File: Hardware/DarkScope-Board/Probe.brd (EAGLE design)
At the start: 65.5 x 80 mm, 50 parts, among them IC1 TL084D, X1 1-227161-0, X4 2540-5

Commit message: Routed Probe Board
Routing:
- net GND: track 0.00 -> 321.7 mm, vias 0 -> 1
- net +5V: track 0.00 -> 157.5 mm, vias 0 -> 3
- net -5V: track 0.00 -> 99.2 mm
- net TRIG: track 0.00 -> 95.5 mm
- net ADCIN: track 0.00 -> 90.4 mm
- net VSENSEL1: track 0.00 -> 90.3 mm
- net TL_PWM: track 0.00 -> 65.7 mm
- net N$8: track 0.00 -> 64.0 mm
- net N$5: track 0.00 -> 61.8 mm
- net CPLSEL: track 0.00 -> 61.0 mm
- net N$6: track 0.00 -> 58.9 mm
- net N$7: track 0.00 -> 48.9 mm
- net N$24: track 0.00 -> 44.3 mm, vias 0 -> 2
- net N$1: track 0.00 -> 41.9 mm
- net N$20: track 0.00 -> 39.0 mm
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- added copper zone on layer 1, net GND
- added copper zone on layer 16, net GND

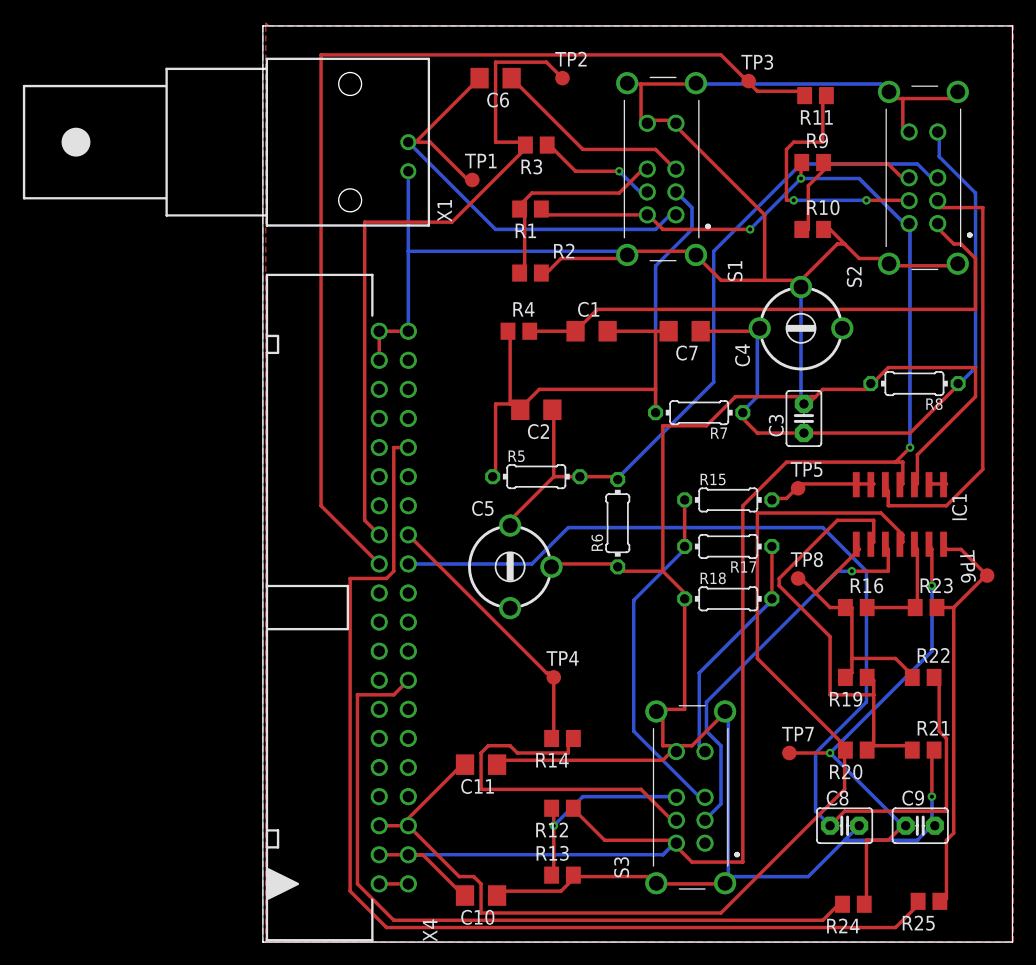
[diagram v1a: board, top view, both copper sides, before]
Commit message: Cleared and Fixed Probe Board's ERC Errors
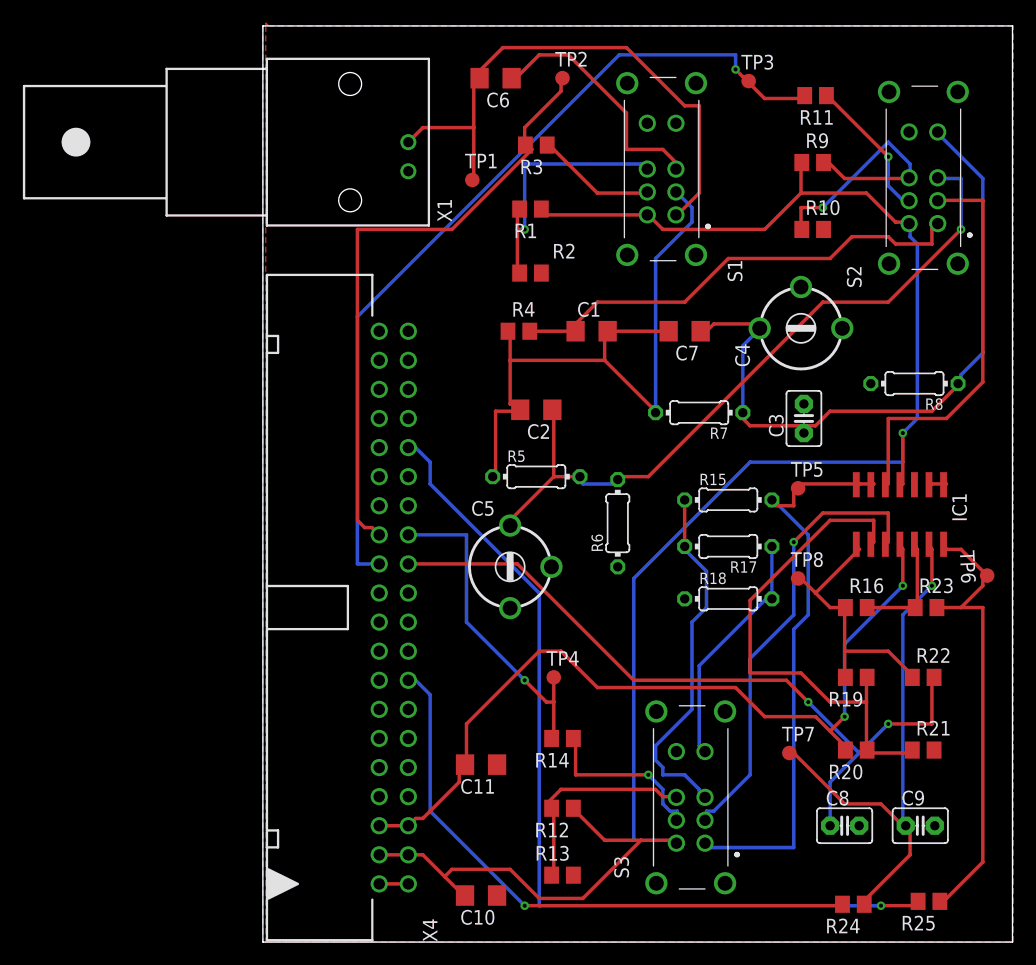
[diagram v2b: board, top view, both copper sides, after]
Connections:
- removed net N$15: IC1.6, IC1.7, R15.2, TP5.TP
- removed net N$19: S3.1
- new net N$18: IC1.6, IC1.7, R15.2, S3.1, TP5.TP
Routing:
- net GND: track 321.7 -> 0.00 mm, vias 1 -> 0
- net N$18: track 0.00 -> 51.9 mm
- net -5V: track 99.2 -> 72.5 mm, vias 0 -> 2
- net ADCIN: track 90.4 -> 65.1 mm, vias 0 -> 2
- net TRIG: track 95.5 -> 78.5 mm, vias 0 -> 1
- net N$14: track 31.2 -> 15.1 mm, vias 0 -> 1
- net VSENSEL1: track 90.3 -> 74.5 mm, vias 0 -> 1
- net TL_PWM: track 65.7 -> 52.0 mm, vias 0 -> 1
- net N$12: track 22.8 -> 12.5 mm, vias 2 -> 1
- net N$15: track 10.1 -> 0.00 mm
- net N$11: track 15.1 -> 23.9 mm, vias 0 -> 1
- net N$7: track 48.9 -> 41.4 mm
- net N$1: track 41.9 -> 49.2 mm
- net CPLSEL: track 61.0 -> 53.8 mm
- net N$16: track 34.4 -> 40.0 mm
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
